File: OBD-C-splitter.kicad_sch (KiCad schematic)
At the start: 11 parts, among them J1 Type-C Plug, J2 Type-C Receptacle, J3 Type-C Receptacle

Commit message: Order matters
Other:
- note added: "J1 is direct J2 is flipps rx/tx with the cable J3 is direct (cable flipping is cancelled out by the PCB) So harness box goes to J2. - Effectively we want to flip only once - with the cable - like in the normal setup."
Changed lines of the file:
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@@
+		)
+	)
+	(text "J1 is direct\nJ2 is flipps rx/tx with the cable\nJ3 is direct (cable flipping is cancelled out by the PCB)\n\nSo harness box goes to J2.  - Effectively we want to flip only once - with the cable - like in the normal setup. \n"
+		(exclude_from_sim no)
+		(at 112.522 26.162 0)
+		(effects
+			(font
+				(size 1.27 1.27)
+			)
+			(justify left)
 		)
 	)

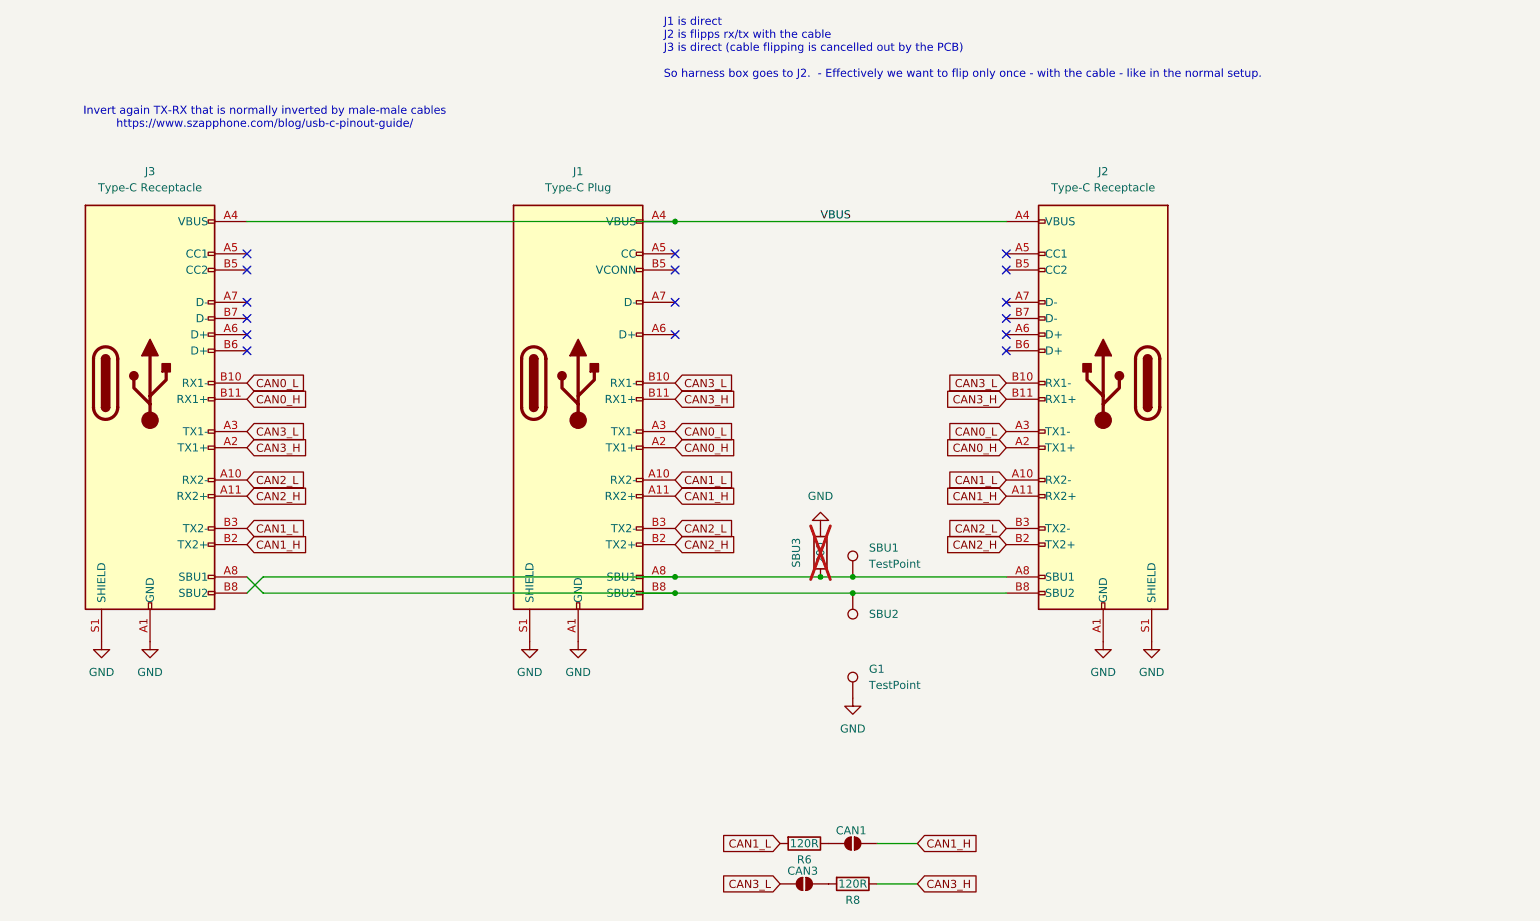
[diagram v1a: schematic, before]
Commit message: Fixed CAN labels and termination resistors and sbu
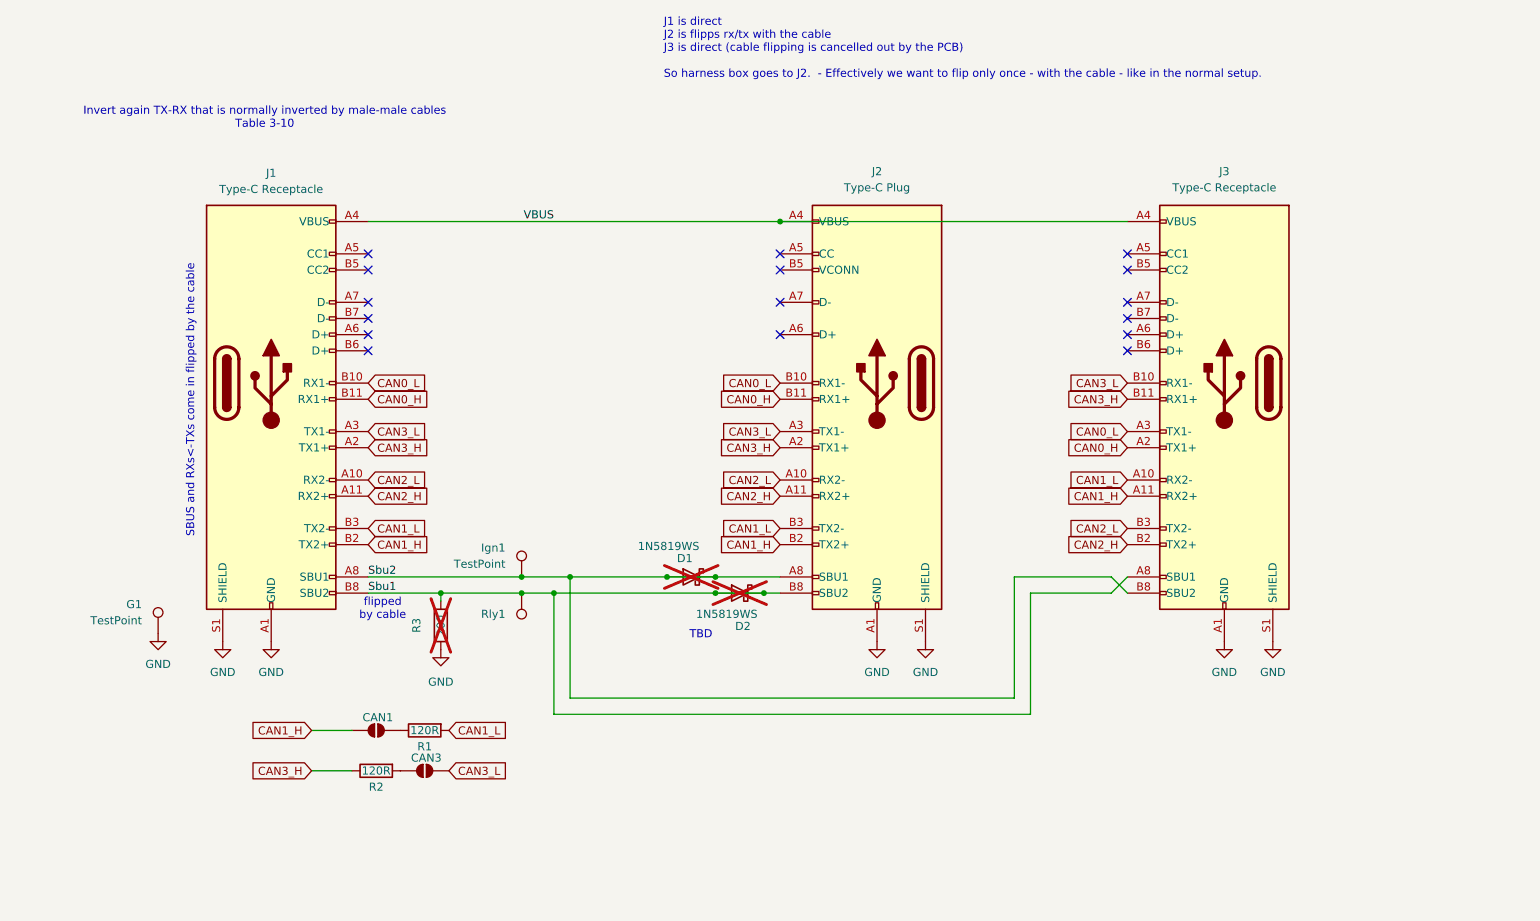
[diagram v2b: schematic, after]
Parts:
- added D1, D2: 1N5819WS, Diode_SMD:D_SOD-323, symbol Diode:1N5819
- renumbered SBU1 to Ign1, J2 to J1, J1 to J2, R6 to R1, R8 to R2, SBU3 to R3, SBU2 to Rly1
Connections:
- net CAN0_H: now also J1.B11 (RX1+), J2.B11 (RX1+), J3.A2 (TX1+); no longer J1.A2 (TX1+), J2.A2 (TX1+), J3.B11 (RX1+)
- net CAN0_L: now also J1.B10 (RX1-), J2.B10 (RX1-), J3.A3 (TX1-); no longer J1.A3 (TX1-), J2.A3 (TX1-), J3.B10 (RX1-)
- net CAN1_H: now also J1.B2 (TX2+), J2.B2 (TX2+), J3.A11 (RX2+); no longer J1.A11 (RX2+), J2.A11 (RX2+), J3.B2 (TX2+)
- net CAN1_L: now also J1.B3 (TX2-), J2.B3 (TX2-), J3.A10 (RX2-); no longer J1.A10 (RX2-), J2.A10 (RX2-), J3.B3 (TX2-)
- net CAN2_H: now also J1.A11 (RX2+), J2.A11 (RX2+), J3.B2 (TX2+); no longer J1.B2 (TX2+), J2.B2 (TX2+), J3.A11 (RX2+)
- net CAN2_L: now also J1.A10 (RX2-), J2.A10 (RX2-), J3.B3 (TX2-); no longer J1.B3 (TX2-), J2.B3 (TX2-), J3.A10 (RX2-)
- net CAN3_H: now also J1.A2 (TX1+), J2.A2 (TX1+), J3.B11 (RX1+); no longer J1.B11 (RX1+), J2.B11 (RX1+), J3.A2 (TX1+)
- net CAN3_L: now also J1.A3 (TX1-), J2.A3 (TX1-), J3.B10 (RX1-); no longer J1.B10 (RX1-), J2.B10 (RX1-), J3.A3 (TX1-)
- net Sbu2: now reaches Ign1.1, J1.A8 (SBU1), J2.A8 (SBU1), J3.B8 (SBU2)
- net Sbu2: now also D1.1 (K), D1.2 (A); no longer R3.1
- net Sbu1: now reaches J1.B8 (SBU2), J2.B8 (SBU2), J3.A8 (SBU1), Rly1.1
- net Sbu1: now also R3.1, D2.1 (K), D2.2 (A)
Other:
- note added: "Invert again TX-RX that is normally inverted by male-male cables Table 3-10"
- note added: "SBUS and RXs<-TXs come in flipped by the cable"
- note added: "TBD"
- note added: "flipped by cable"
- note removed: "Invert again TX-RX that is normally inverted by male-male cables https://www.szapphone.com/blog/usb-c-pinout-guide/"
- moved on the sheet: CAN1, CAN3, G1, Ign1, J1, J2, J3, R1, R2, R3, Rly1
